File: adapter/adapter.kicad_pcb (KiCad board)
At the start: 2 copper layers, 93.5 x 50.9 mm, 30 parts, among them J1 DF3A-2P-2DSA, J10 Ribbon, J11 Ribbon, J12 Ribbon, J2 DF3A-2P-2DSA, J9 Ribbon, SW1 CAS-120TA, SW2 CAS-120TA, U1 nice_nano, U2 nice_nano

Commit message: Cleanup the silk
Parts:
- removed kibuzzard-61F01A92 (x2): G***, kibuzzard-61F01A92
- removed kibuzzard-61F01C84 (x2): G***, kibuzzard-61F01C84
- moved kibuzzard-61F01B61 0.61 mm to (133.7, 70.1)
- moved kibuzzard-61F01B61 0.61 mm to (133.6, 70.1)
- moved kibuzzard-6208EFFE 0.13 mm to (177.8, 69.9)
- moved kibuzzard-6208EFFE 0.13 mm to (177.8, 70.1)
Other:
- board text removed: "Install Elite-C upside down together with ribbon cables and trs jack on this side. Push button on the opposite."

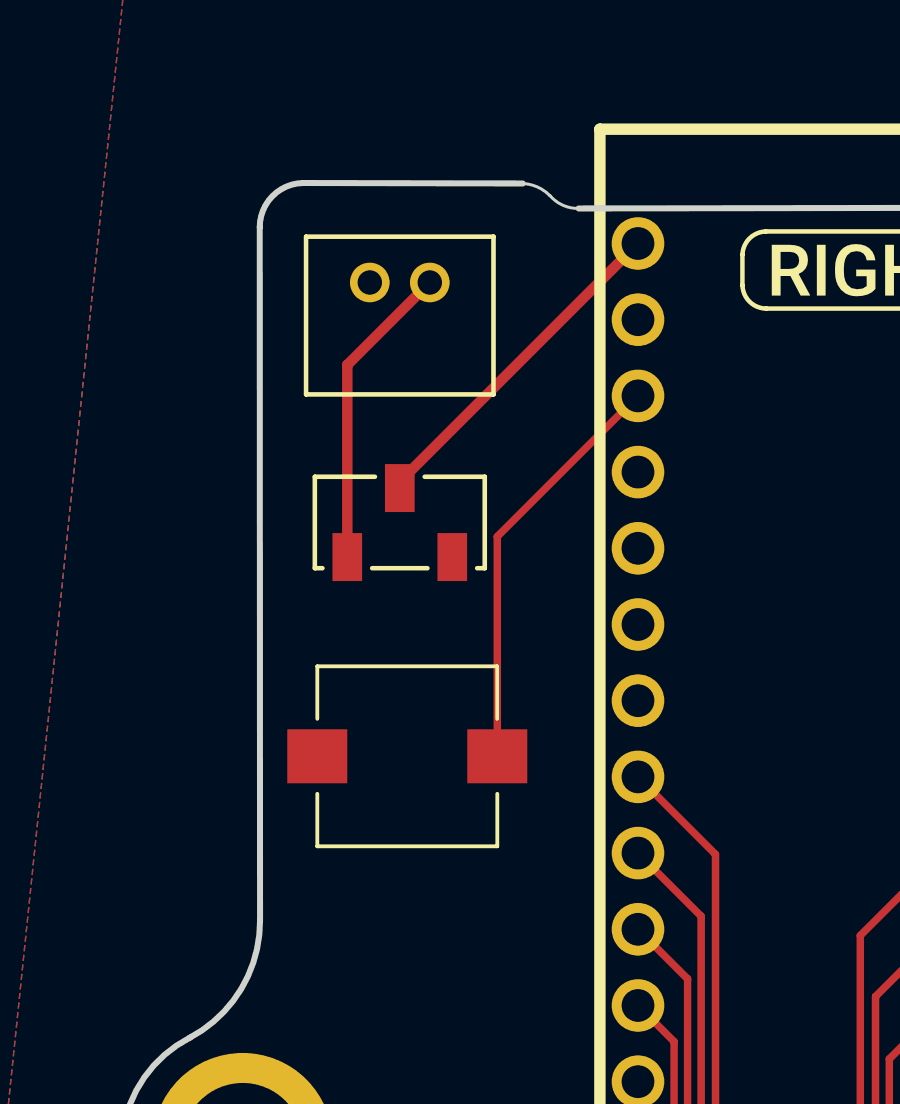
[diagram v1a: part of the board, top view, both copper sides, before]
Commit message: Removed the powerswitch, reset button and jst connector + fixed the corner extention
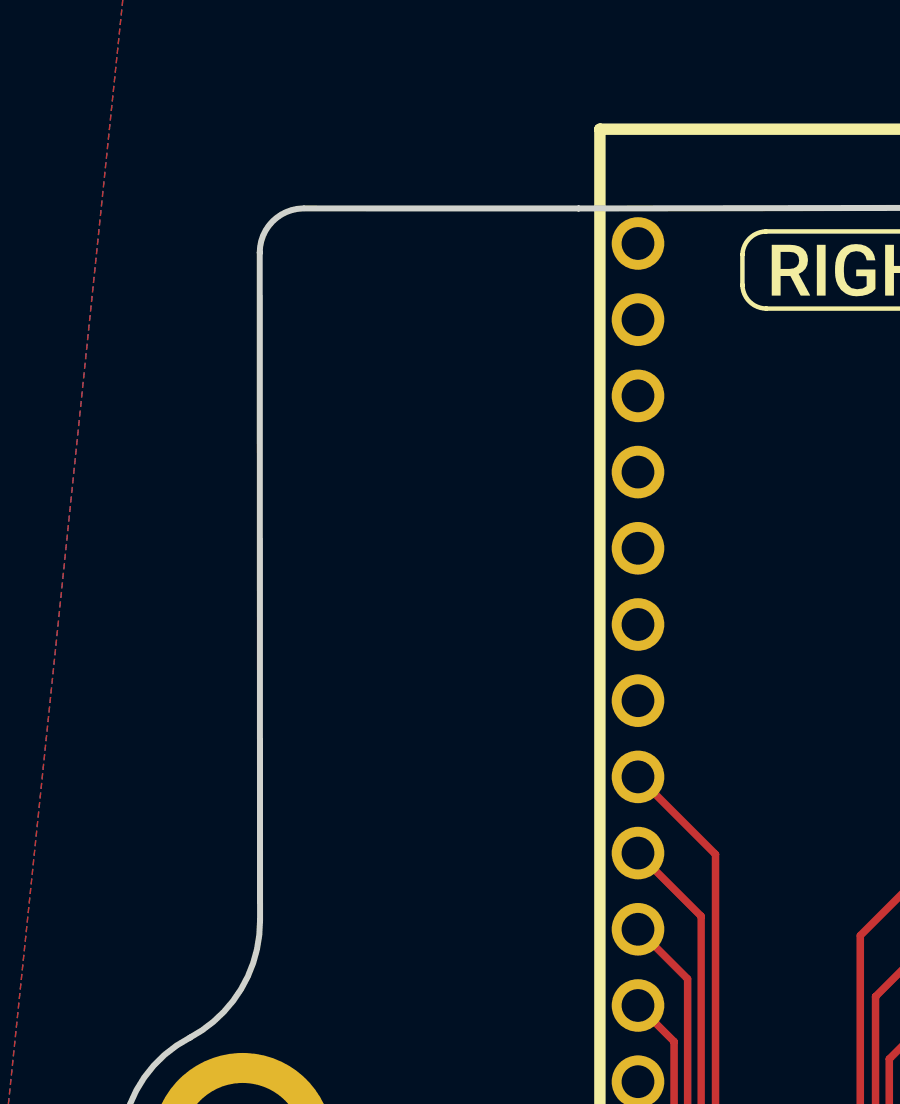
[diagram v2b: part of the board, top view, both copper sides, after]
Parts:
- removed J1: DF3A-2P-2DSA, Library:DF3A_2P_2DSA
- removed S1: TL9210AF180Q, Library:SW_TL9210AF180Q
- removed SW1: CAS-120TA, Library:CAS-120A_NDC
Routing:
- net rst_l: track 14.0 -> 0.00 mm
- net bat_sw_l: track 11.4 -> 0.00 mm
- net bat_l: track 10.3 -> 0.00 mm
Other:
- outline, holes or cut-outs redrawn

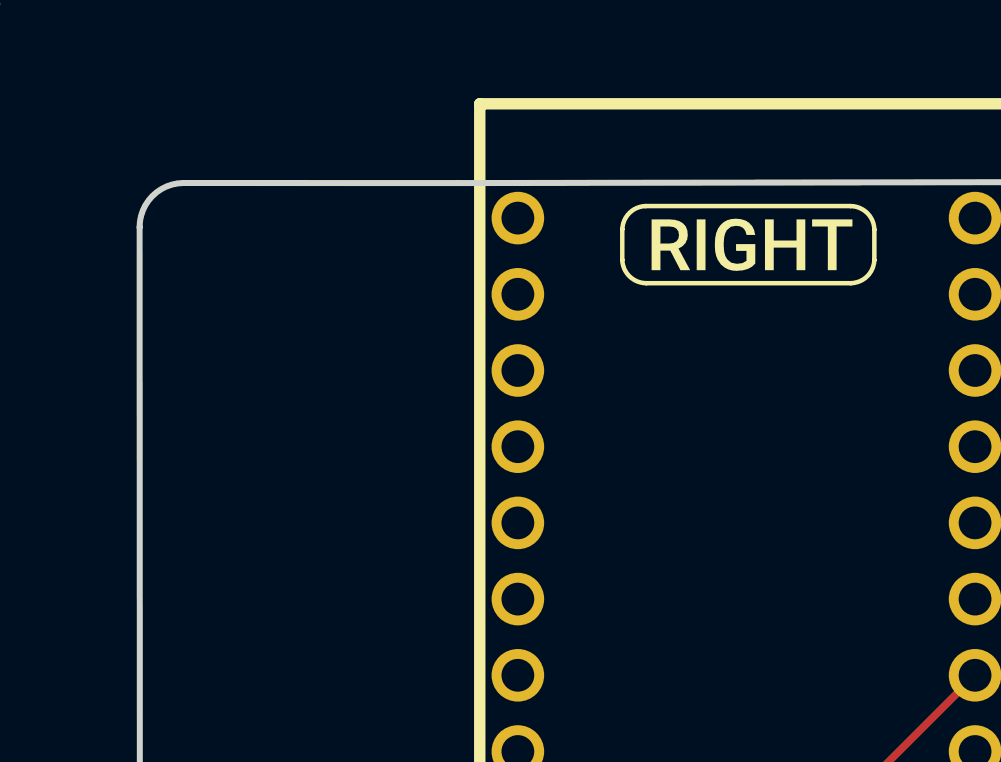
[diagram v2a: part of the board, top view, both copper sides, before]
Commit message: Add custom reset switch
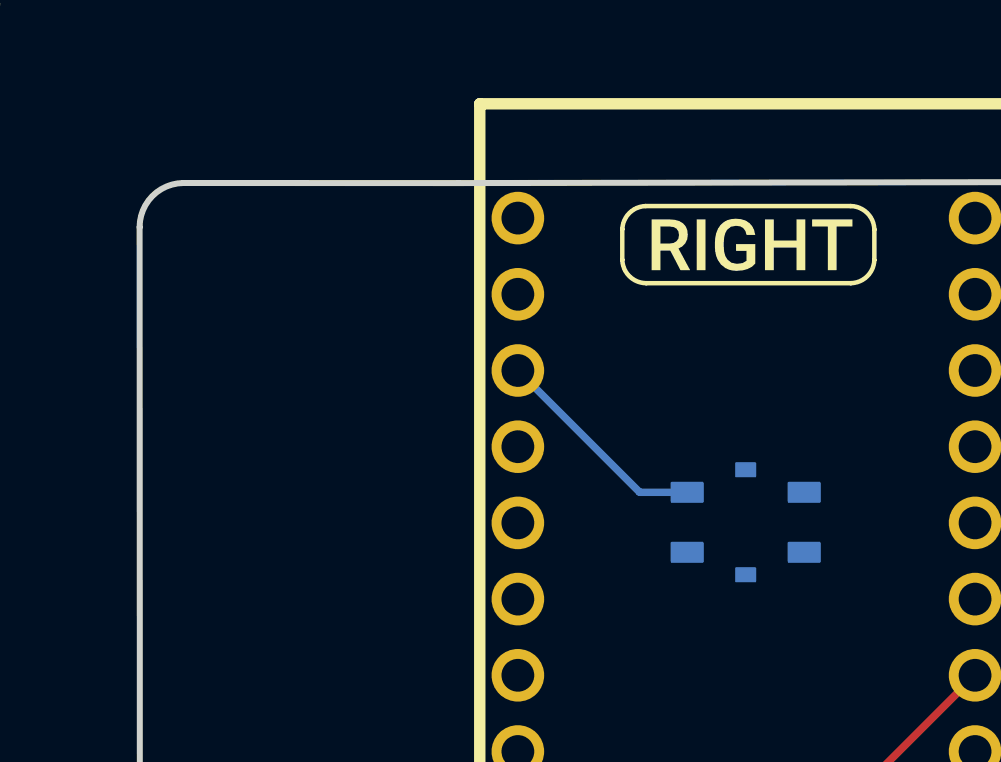
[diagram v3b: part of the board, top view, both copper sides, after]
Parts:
- added SW1: SW_Push, Library:SW_Tactile_3x3_SMD_H1p5, B.Cu at (133.5, 79.3)
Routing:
- net rst_l: track 0.00 -> 7.33 mm
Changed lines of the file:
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@@
 		(embedded_fonts no)
 	)
+	(footprint "Library:SW_Tactile_3x3_SMD_H1p5"
+		(layer "B.Cu")
+		(at 133.5336 79.3402 180)
+		(property "Reference" "SW1"
+			(at 0 0.5 0)
+			(unlocked yes)
+			(layer "B.SilkS")
+			(hide yes)
+			(effects
+				(font
+					(size 1 1)
+					(thickness 0.1)
+				)
+				(justify mirror)
+			)
+		)
+		(property "Value" "SW_Push"
+			(at 0 5 0)
+			(unlocked yes)
+			(layer "B.Fab")
+			(effects
+				(font
+					(size 1 1)
+					(thickness 0.15)
+				)
+				(justify mirror)
+			)
+		)
+		(property "Datasheet" "~"
+			(at 0 0 0)
+			(unlocked yes)
+			(layer "B.Fab")
+			(hide yes)
+			(effects
+				(font
+					(size 1 1)
+					(thickness 0.15)
+				)
+				(justify mirror)
+			)
+		)
+		(property "Description" "Push button switch, generic, two pins"
+			(at 0 0 0)
+			(unlocked yes)
+			(layer "B.Fab")
+			(hide yes)
+			(effects
+				(font
+					(size 1 1)
+					(thickness 0.15)
+				)
+				(justify mirror)
+			)
+		)
+		(sheetname "/")
+		(sheetfile "adapter.kicad_sch")
+		(attr smd)
+		(fp_line
+			(start 2.65 1.5)
+			(end 2.65 0.7)
+			(stroke
+				(width 0.1)
+				(type solid)
+			)
+			(layer "B.SilkS")
+		)
+		(fp_line
+			(start 2.65 1.5)
+			(end 1.45 1.5)
+			(stroke
+				(width 0.1)
+				(type solid)
+			)
+			(layer "B.SilkS")
+		)
+		(fp_line
+			(start 2.65 -0.69)
+			(end 2.65 -1.49)
+			(stroke
+				(width 0.1)
+				(type solid)
+			)
+			(layer "B.SilkS")
+		)
+		(fp_line
+			(start 2.65 -1.5)
+			(end 1.45 -1.5)
+			(stroke
+				(width 0.1)
+				(type solid)
+			)
+			(layer "B.SilkS")
+		)
+		(fp_line
+			(start -2.65 1.5)
+			(end -1.45 1.5)
+			(stroke
+				(width 0.1)
+				(type solid)
+			)
+			(layer "B.SilkS")
+		)
+		(fp_line
+			(start -2.65 0.7)
+			(end -2.65 1.5)
+			(stroke
+				(width 0.1)
+				(type solid)
+			)
+			(layer "B.SilkS")
+		)
+		(fp_line
+			(start -2.65 -1.5)
+			(end -1.45 -1.5)
+			(stroke
+				(width 0.1)
+				(type solid)
+			)
+			(layer "B.SilkS")
+		)
+		(fp_line
+			(start -2.65 -1.5)
+			(end -2.65 -0.7)
+			(stroke
+				(width 0.1)
+				(type solid)
+			)
+			(layer "B.SilkS")
+		)
+		(pad "" smd roundrect
+			(at 0 -1.75 180)
+			(size 0.7 0.5)
+			(layers "B.Cu" "B.Mask" "B.Paste")
+			(roundrect_rratio 0.05)
+		)
+		(pad "" smd roundrect
+			(at 0 1.75 180)
+			(size 0.7 0.5)
+			(layers "B.Cu" "B.Mask" "B.Paste")
+			(roundrect_rratio 0.05)
+		)
+		(pad "1" smd roundrect
+			(at -1.95 1 180)
+			(size 1.1 0.7)
+			(layers "B.Cu" "B.Mask" "B.Paste")
+			(roundrect_rratio 0.05)
+			(net 25 "rst_l")
+			(pinfunction "1")
+			(pintype "passive")
+		)
+		(pad "1" smd roundrect
+			(at 1.95 1 180)
+			(size 1.1 0.7)
+			(layers "B.Cu" "B.Mask" "B.Paste")
+			(roundrect_rratio 0.05)
+			(net 25 "rst_l")
+			(pinfunction "1")
+			(pintype "passive")
+		)
+		(pad "2" smd roundrect
+			(at -1.95 -1 180)
+			(size 1.1 0.7)
+			(layers "B.Cu" "B.Mask" "B.Paste")
+			(roundrect_rratio 0.05)
+			(net 23 "GND")
+			(pinfunction "2")
+			(pintype "passive")
+		)
+		(pad "2" smd roundrect
+			(at 1.95 -1 180)
+			(size 1.1 0.7)
+			(layers "B.Cu" "B.Mask" "B.Paste")
+			(roundrect_rratio 0.05)
+			(net 23 "GND")
+			(pinfunction "2")
+			(pintype "passive")
+		)
+		(embedded_fonts no)
+	)
 	(footprint "kibuzzard-61F01940"
 		(layer "B.Cu")
@@
 	(gr_line
 		(start 123.961303 68.03306)
-		(end 114.823289 68.030249)
+		(end 114.777778 68.030235)
 		(stroke
 			(width 0.2)
@@
 	)
 	(segment
+		(start 130.0002 78.3402)
+		(end 125.94 74.28)
+		(width 0.25)
+		(layer "B.Cu")
+		(net 25)
+	)
+	(segment
+		(start 131.5836 78.3402)
+		(end 130.0002 78.3402)
+		(width 0.25)
+		(layer "B.Cu")
+		(net 25)
+	)
+	(segment

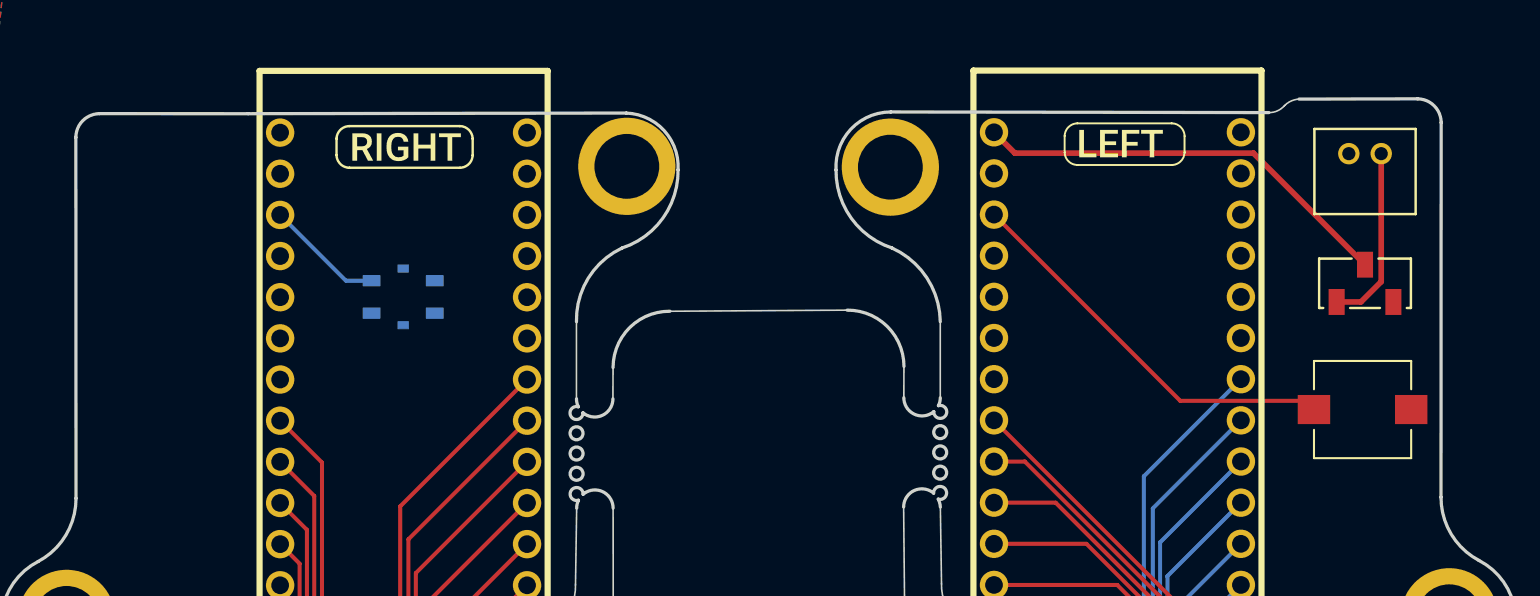
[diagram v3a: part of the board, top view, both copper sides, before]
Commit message: Add JST connectors and cleaned up the PCB
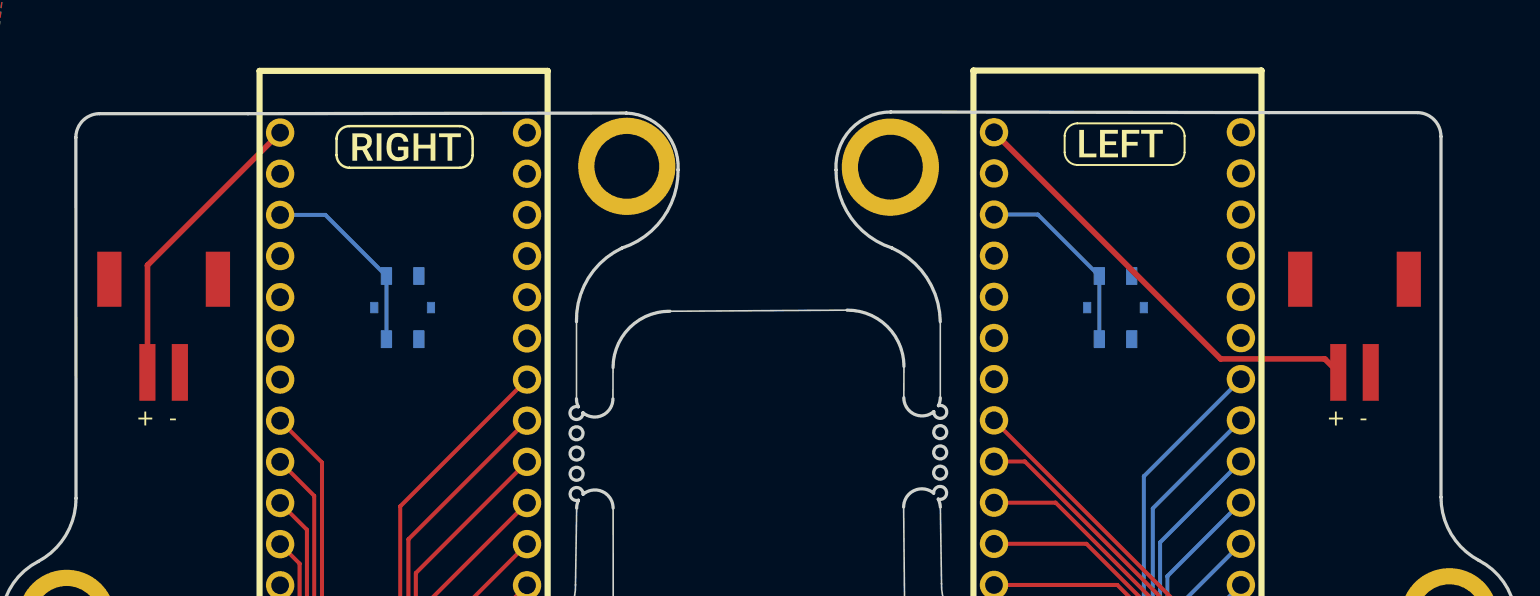
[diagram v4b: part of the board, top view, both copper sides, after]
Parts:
- removed J2: DF3A-2P-2DSA, Library:DF3A_2P_2DSA
- removed S2: TL9210AF180Q, Library:SW_TL9210AF180Q
- added P1: S2B-PH-SM4-TB, Library:JST_S2B-PH-SM4-TB, F.Cu at (118.8, 84.0)
- added P2: S2B-PH-SM4-TB, Library:JST_S2B-PH-SM4-TB, F.Cu at (192.2, 84.0)
- SW2: value CAS-120TA -> SW_Push; footprint Library:CAS-120A_NDC -> Library:SW_Tactile_3x3_SMD_H1p5; moved to B.Cu
- moved SW2 15.5 mm to (177.5, 80.0), turned to -90 degrees
- moved SW1 0.66 mm to (133.5, 80.0), turned to -90 degrees
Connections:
- SW2 pad 1: bat_r -> rst_r
- SW2 pad 2: bat_sw_r -> GND
- U1 pad 24: bat_sw_l -> bat_l
- U2 pad 24: bat_sw_r -> bat_r
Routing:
- net bat_sw_r: track 26.3 -> 0.00 mm
- net bat_l: track 0.00 -> 18.2 mm
- net bat_r: track 11.2 -> 27.4 mm
- net rst_r: track 25.4 -> 12.0 mm
- net rst_l: track 7.33 -> 12.0 mm
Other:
- board size 93.5 x 50.9 mm -> 93.5 x 50.1 mm
- board text added: "+"
- board text added: "-"
- board text removed: "2022 QUENTIN LEBASTARD AND STEFAN KERKMANN"
- board text removed: "BASTARDKB.COM"
- board text removed: "ELITE-C HOLDER 2.1"
- board text removed: "GITHUB.COM/BASTARDKB"
- board text removed: "Licensed under CERN-OHL-W v2"
- board text removed: "Special thanks to: Drashna, Freznel Karl"
